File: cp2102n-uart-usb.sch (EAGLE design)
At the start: 26 parts, among them IC1 CP2102N-A02-GQFN24, J1 USB4105-GF-A, J2 61300611021

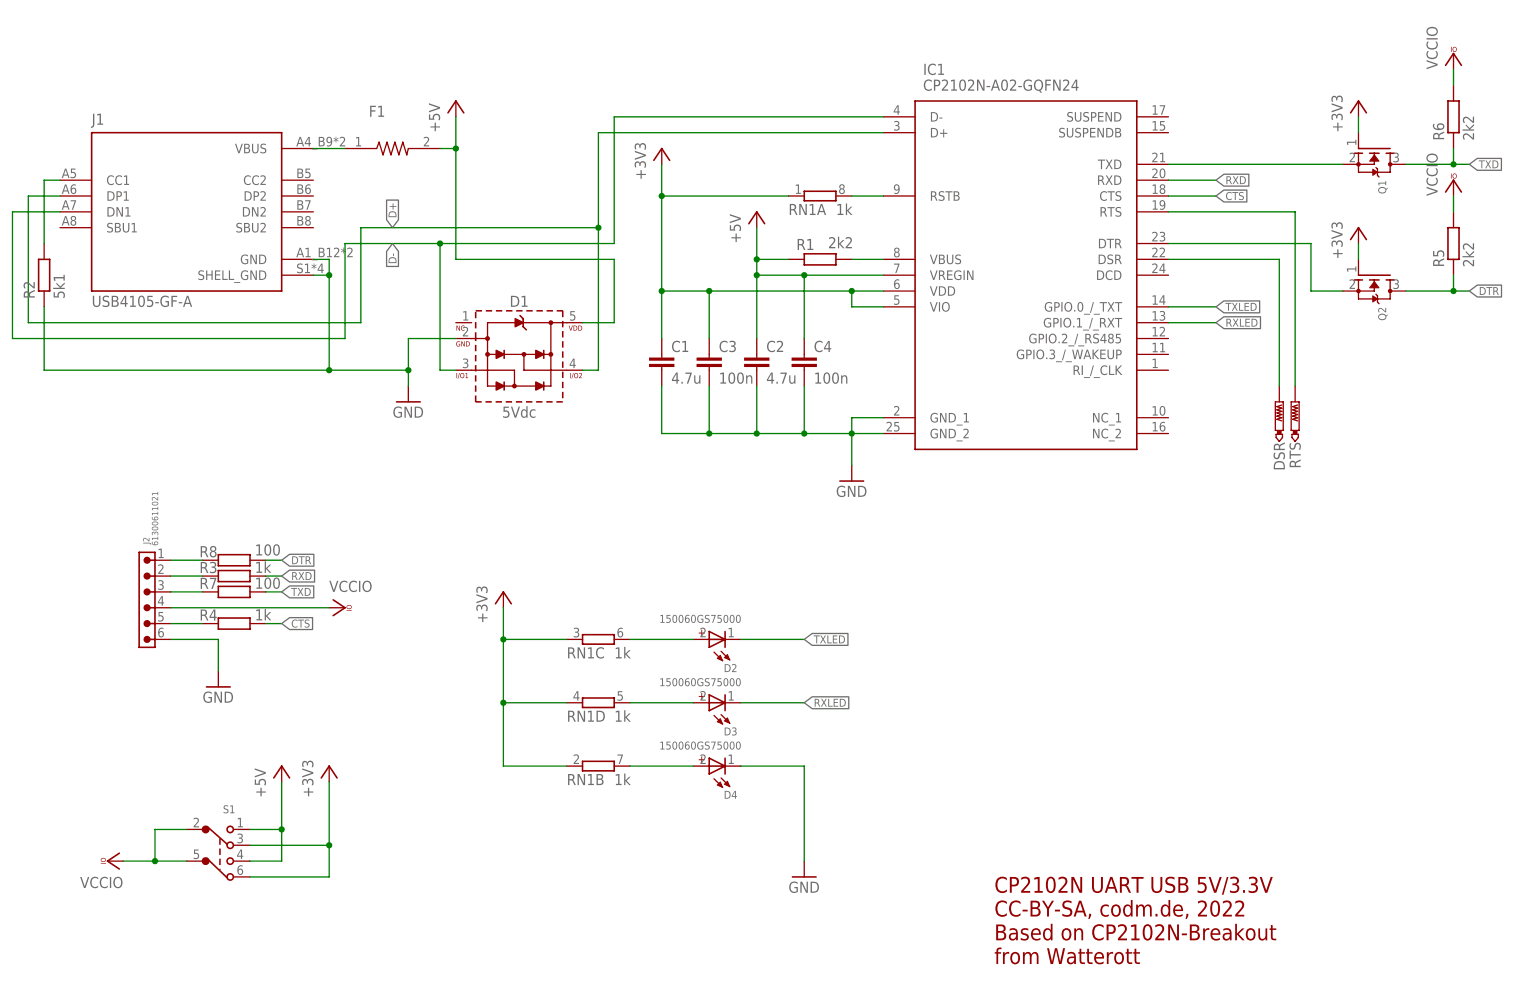
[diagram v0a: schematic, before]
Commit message: added 5k1 to CC2
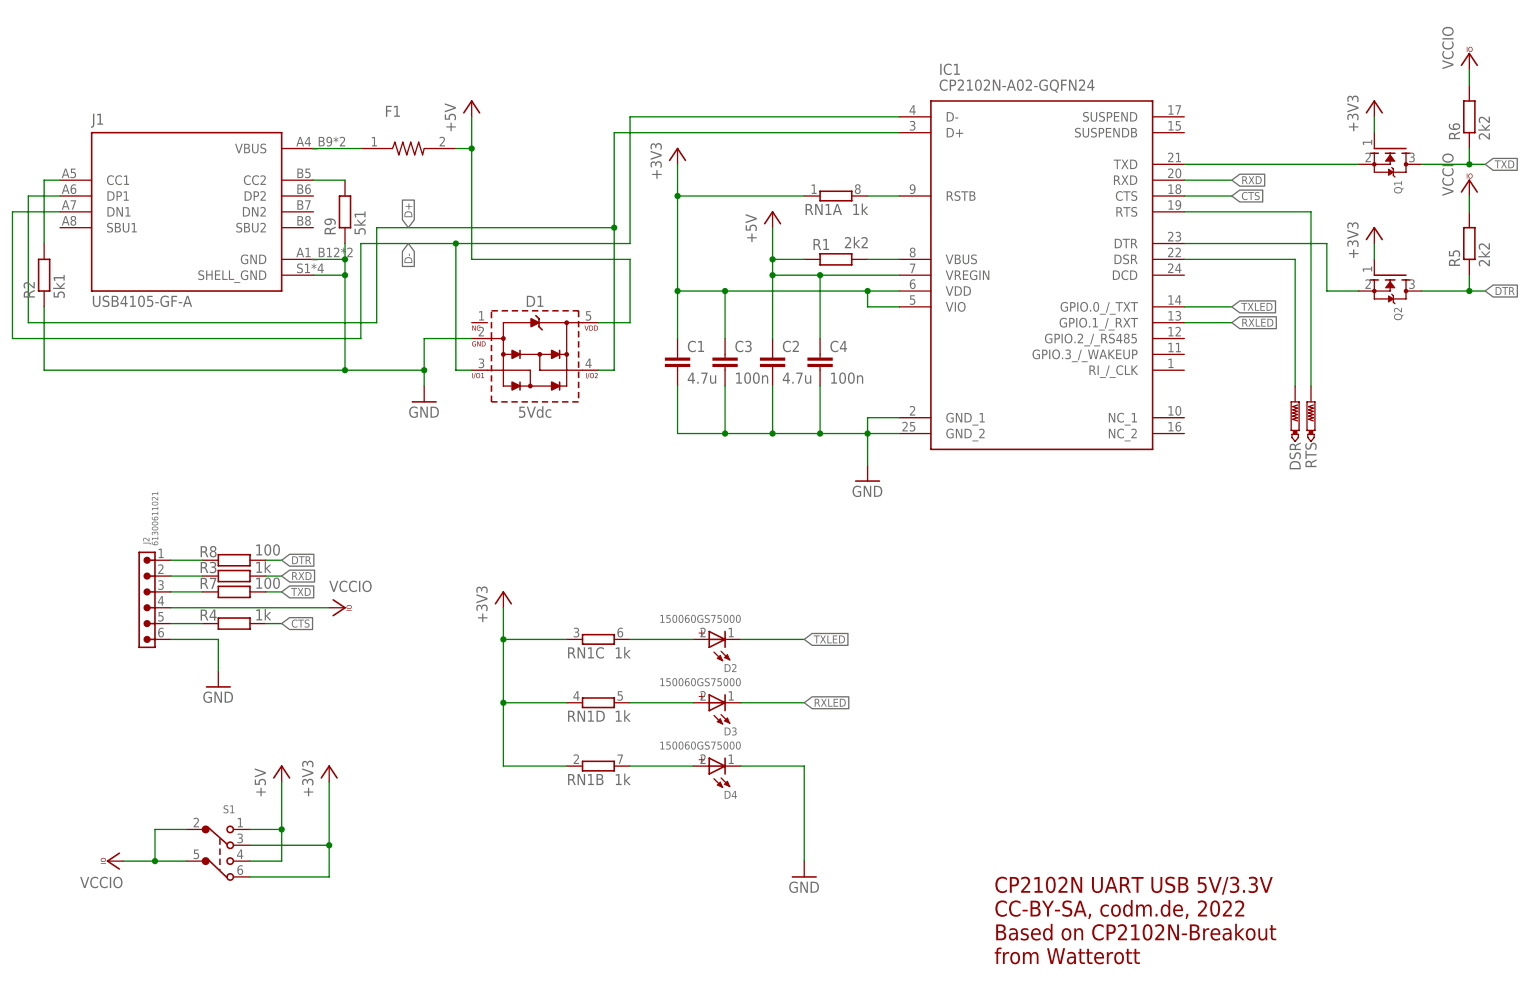
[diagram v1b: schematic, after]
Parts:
- added R9: 5k1, codm:R-EU_R0603RF
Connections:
- new net N$5: J1.CC2, R9.2
- net GND: now also R9.1
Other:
- moved on the sheet: C1, C2, C3, C4, D1, DSR, F1, IC1, Q1, Q2, R1, R5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
